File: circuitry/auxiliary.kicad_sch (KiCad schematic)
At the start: 17 parts, among them P31 JST XH 3pin, P32 JST XH 3pin, P33 JST XH 3pin, P34 JST XH 3pin

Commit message: fix: Resolve circuit signal issues
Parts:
- added R4, R5, R6: 330, symbol Device:R
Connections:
- net +3V3: now also HUI1.1 (VDD), S3.AD0; no longer S4.1 (VCC)
- net +5V: now also S4.1 (VCC); no longer HUI1.1 (VDD)
- net at MA3.7 (A6): now also R4.1; no longer S3.SCL
- net at MA3.8 (A7): now also R5.1; no longer S3.SDA
- net at MA2.12 (B8), MCU1.50: no longer MA1.4 (DO)
- net at HUI1.6 (SDI), MA2.5 (A4): now also HUI1.12 (TDI)
- net at HUI1.13 (TDO), MA2.9 (A8): now also R6.1
- new net: R4.2, S3.SCL
- new net: R5.2, S3.SDA
- new net: MA1.4 (DO), R6.2
- no-connect marks 72 -> 70
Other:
- moved on the sheet: HUI1

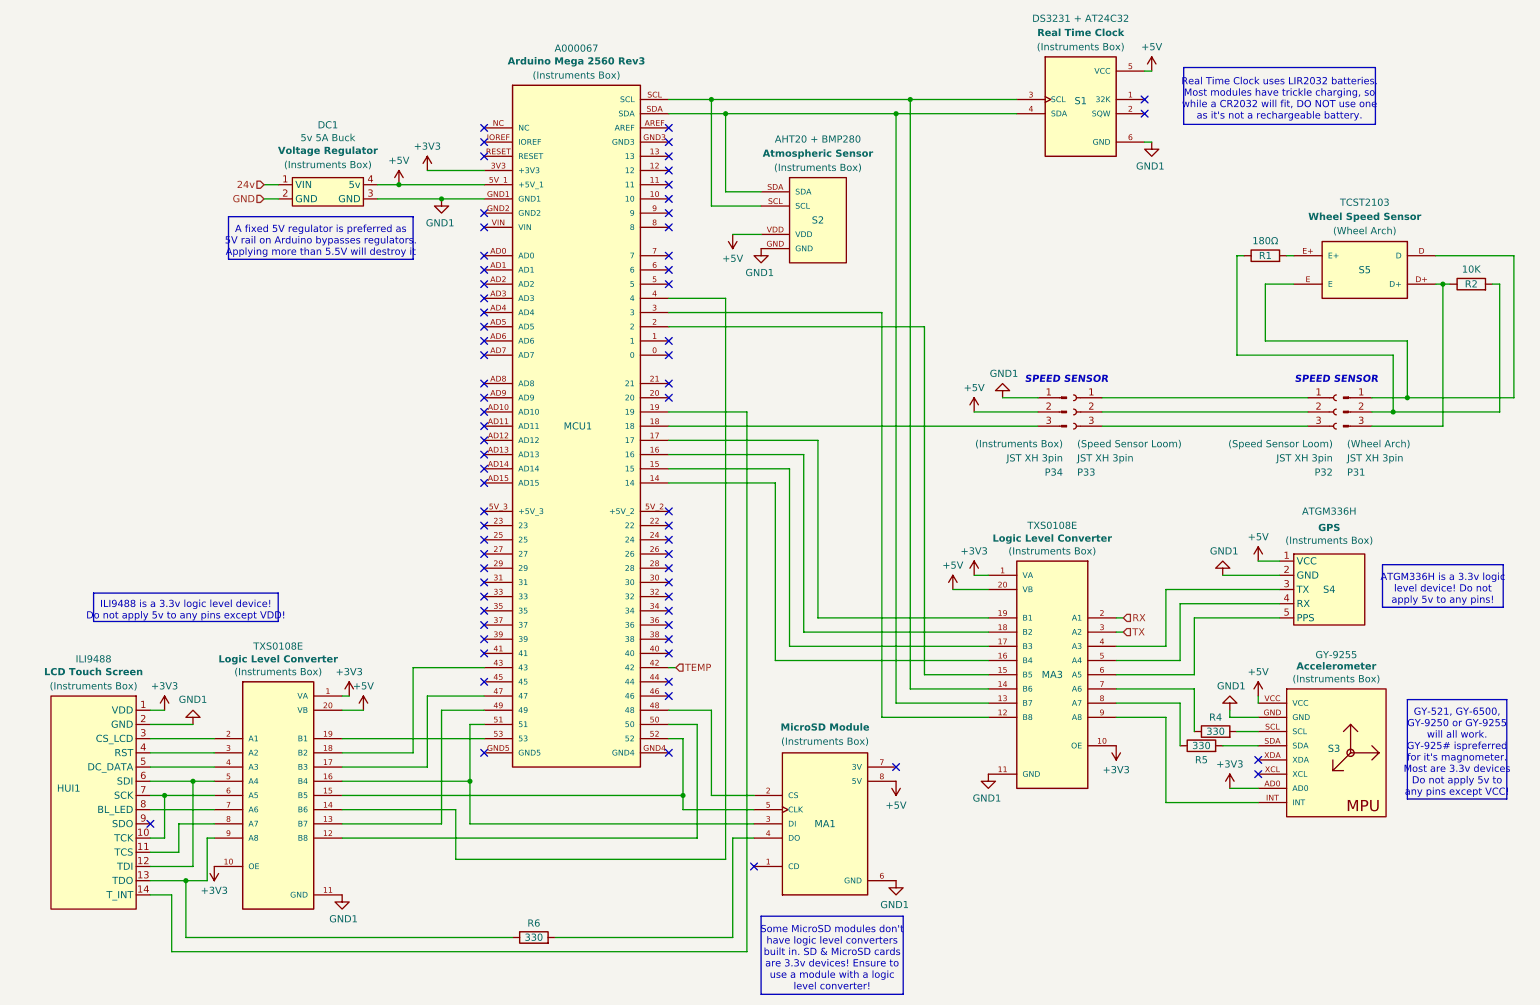
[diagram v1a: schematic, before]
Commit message: fix: Revise circuit plugs & resistors
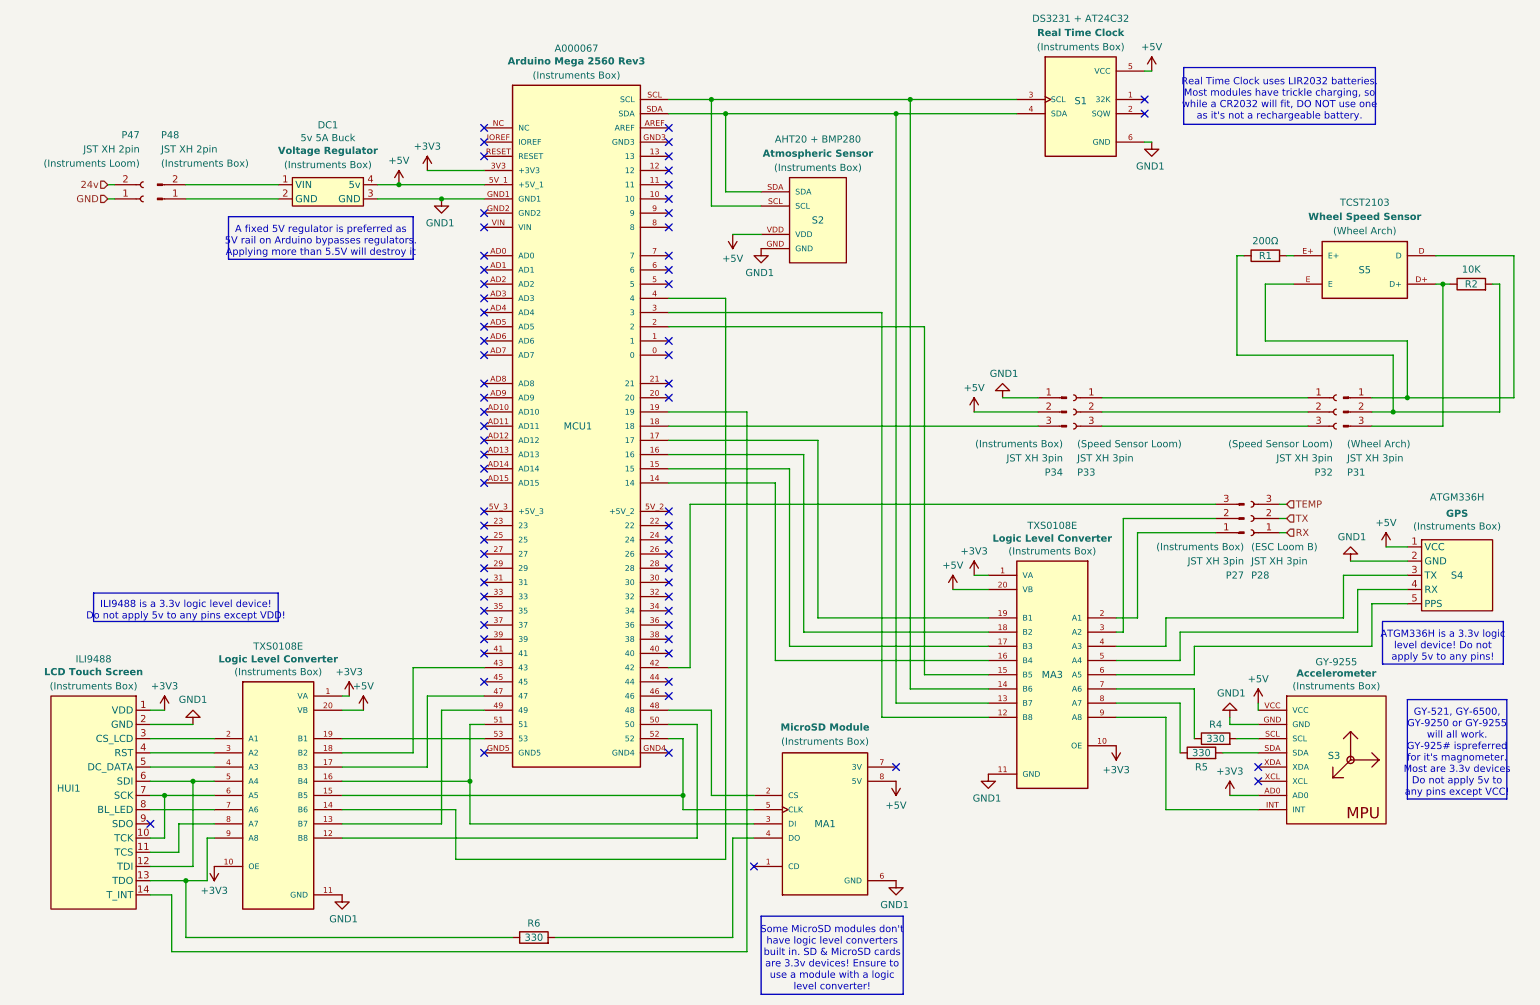
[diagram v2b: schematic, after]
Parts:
- added P27: JST XH 3pin, symbol Connector:Conn_01x03_Pin
- added P28: JST XH 3pin, symbol Connector:Conn_01x03_Socket
- added P47: JST XH 2pin, symbol Connector:Conn_01x02_Socket
- added P48: JST XH 2pin, symbol Connector:Conn_01x02_Pin
- R1: value 180Ω -> 200Ω
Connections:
- net 24v: now also P47.2 (Pin_2); no longer DC1.1 (VIN)
- net GND: now also P47.1 (Pin_1); no longer DC1.2 (GND)
- net RX: now also P28.1 (Pin_1); no longer MA3.2 (A1)
- net TEMP: now also P28.3 (Pin_3); no longer MCU1.42
- net TX: now also P28.2 (Pin_2); no longer MA3.3 (A2)
- new net: DC1.1 (VIN), P48.2 (Pin_2)
- new net: DC1.2 (GND), P48.1 (Pin_1)
- new net: MA3.2 (A1), P27.1 (Pin_1)
- new net: MA3.3 (A2), P27.2 (Pin_2)
- new net: MCU1.42, P27.3 (Pin_3)
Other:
- note removed: "SPEED SENSOR"
- moved on the sheet: R4, R5, S3, S4

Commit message: fix: Add 4.7k onewire pullup
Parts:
- added R7: 4.7k, symbol Device:R
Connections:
- net +5V: now also R7.2
- net at MCU1.42, P27.3 (Pin_3): now also R7.1
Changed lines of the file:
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@@
 		(title "Instruments Box Circuit")
 		(date "2026-06-28")
-		(rev "4")
+		(rev "4.1")
 		(company "Wackadoos F24+")
 		(comment 1 "Connector Convention: Pin 1 = GND. Pin 2 = VCC. Further pins are signal")
@@
 	)
 	(junction
+		(at 162.56 106.68)
+		(diameter 0)
+		(color 0 0 0 0)
+	)
+	(junction
 		(at 43.18 173.99)
 		(diameter 0)
@@
 	(wire
 		(pts
-			(xy 227.33 106.68) (xy 133.35 106.68)
+			(xy 133.35 106.68) (xy 162.56 106.68)
 		)
 		(stroke
@@
 	(wire
 		(pts
+			(xy 162.56 106.68) (xy 227.33 106.68)
+		)
+		(stroke
+			(width 0)
+			(type default)
+		)
+	)
+	(wire
+		(pts
 			(xy 132.08 158.75) (xy 132.08 161.29)
 		)
@@
 	)
 	(symbol
+		(lib_id "power:+5V")
+		(at 162.56 99.06 0)
+		(mirror y)
+		(unit 1)
+		(body_style 1)
+		(exclude_from_sim no)
+		(in_bom yes)
+		(on_board yes)
+		(in_pos_files yes)
+		(dnp no)
+		(property "Reference" "#PWR044"
+			(at 162.56 102.87 0)
+			(hide yes)
+			(show_name no)
+			(do_not_autoplace no)
+			(effects
+				(font
+					(size 1.27 1.27)
+				)
+			)
+		)
+		(property "Value" "+5V"
+			(at 162.56 94.742 0)
+			(show_name no)
+			(do_not_autoplace no)
+			(effects
+				(font
+					(size 1.27 1.27)
+				)
+			)
+		)
+		(property "Footprint" ""
+			(at 162.56 99.06 0)
+			(hide yes)
+			(show_name no)
+			(do_not_autoplace no)
+			(effects
+				(font
+					(size 1.27 1.27)
+				)
+			)
+		)
+		(property "Datasheet" ""
+			(at 162.56 99.06 0)
+			(hide yes)
+			(show_name no)
+			(do_not_autoplace no)
+			(effects
+				(font
+					(size 1.27 1.27)
+				)
+			)
+		)
+		(property "Description" "Power symbol creates a global label with name \"+5V\""
+			(at 162.56 99.06 0)
+			(hide yes)
+			(show_name no)
+			(do_not_autoplace no)
+			(effects
+				(font
+					(size 1.27 1.27)
+				)
+			)
+		)
+		(pin "1"
+		)
+		(instances
+			(project "instruments"
+				(path "/7b3a8acc-a7bf-4991-b6ab-1771768f1043/48c869f0-37c7-4f58-87f7-eb0e41b18d06"
+					(reference "#PWR044")
+					(unit 1)
+				)
+			)
+		)
+	)
+	(symbol
 		(lib_id "Device:R")
 		(at 105.41 184.15 90)
@@
 					(unit 1)
 				)
+			)
+		)
+	)
+	(symbol
+		(lib_id "Device:R")
+		(at 162.56 102.87 180)
+		(unit 1)
+		(body_style 1)
+		(exclude_from_sim no)
+		(in_bom yes)
+		(on_board yes)
+		(in_pos_files yes)
+		(dnp no)
+		(property "Reference" "R7"
+			(at 160.02 102.87 90)
+			(show_name no)
+			(do_not_autoplace no)
+			(effects
+				(font
+					(size 1.27 1.27)
+				)
+			)
+		)
+		(property "Value" "4.7k"
+			(at 162.56 102.87 90)
+			(show_name no)
+			(do_not_autoplace no)
+			(effects
+				(font
+					(size 1.27 1.27)
+				)
+			)
+		)
+		(property "Footprint" ""
+			(at 164.338 102.87 90)
+			(hide yes)
+			(show_name no)
+			(do_not_autoplace no)
+			(effects
+				(font
+					(size 1.27 1.27)
+				)
+			)
+		)
+		(property "Datasheet" ""
+			(at 162.56 102.87 0)
+			(hide yes)
+			(show_name no)
+			(do_not_autoplace no)
+			(effects
+				(font
+					(size 1.27 1.27)
+				)
+			)
+		)
+		(property "Description" "Resistor"
+			(at 162.56 102.87 0)
+			(hide yes)
+			(show_name no)
+			(do_not_autoplace no)
+			(effects
+				(font
+					(size 1.27 1.27)
+				)
+			)
+		)
+		(pin "1"
+		)
+		(pin "2"
+		)
+		(instances
+			(project "instruments"
+				(path "/7b3a8acc-a7bf-4991-b6ab-1771768f1043/48c869f0-37c7-4f58-87f7-eb0e41b18d06"
+					(reference "R7")
+					(unit 1)
+				)
